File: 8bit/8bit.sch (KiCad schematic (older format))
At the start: 0 parts

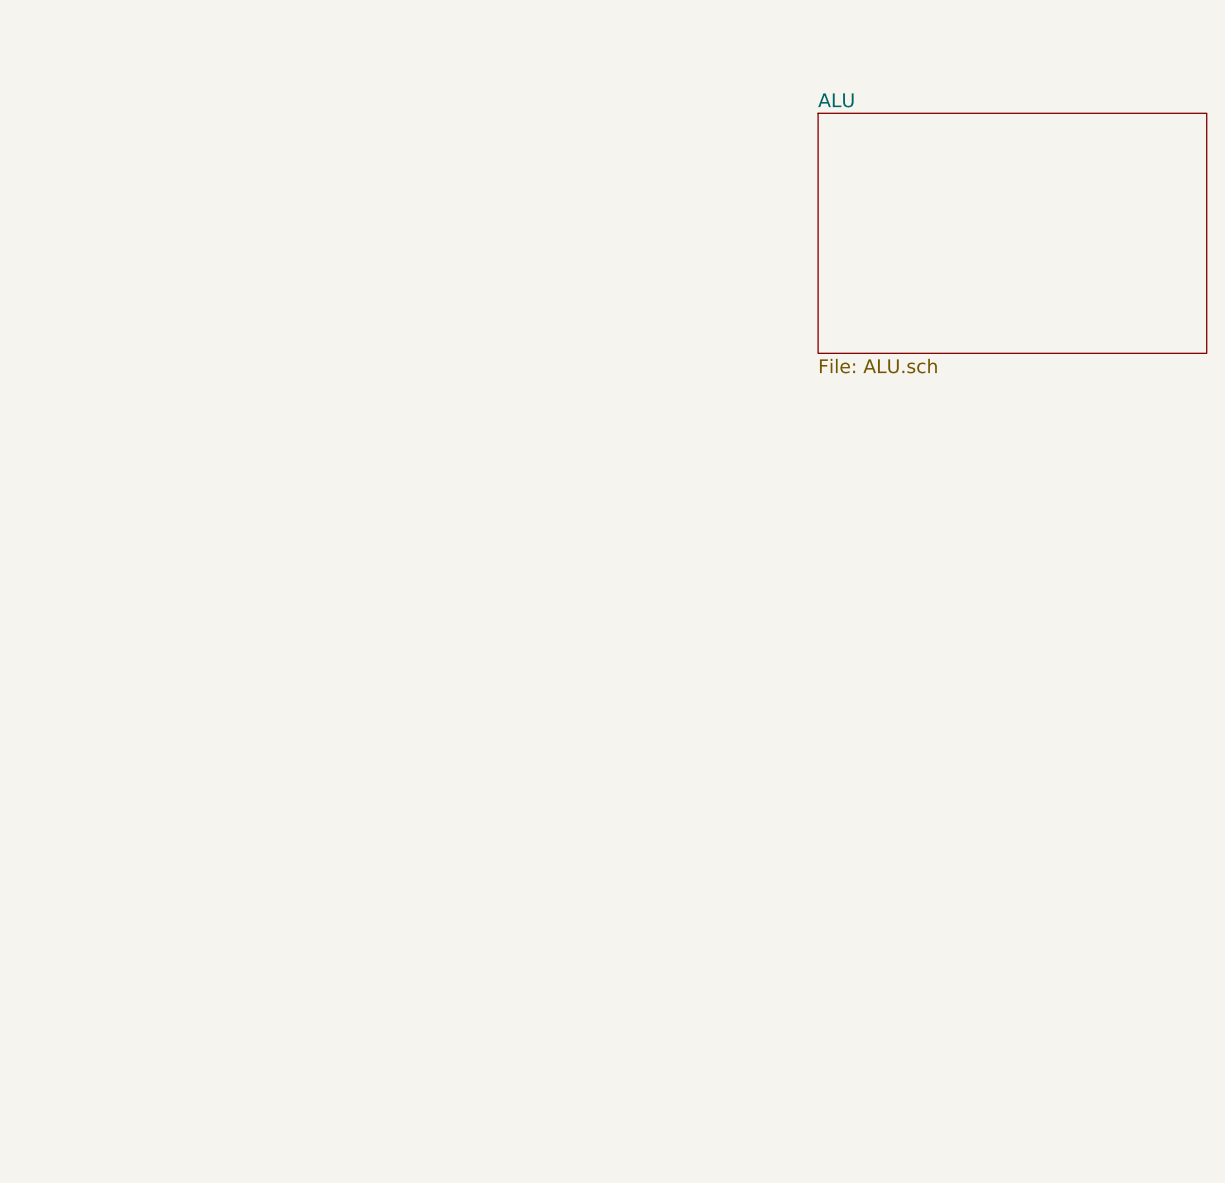
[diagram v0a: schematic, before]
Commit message: Added top level hierarchical diagram
Created 1-bit counter
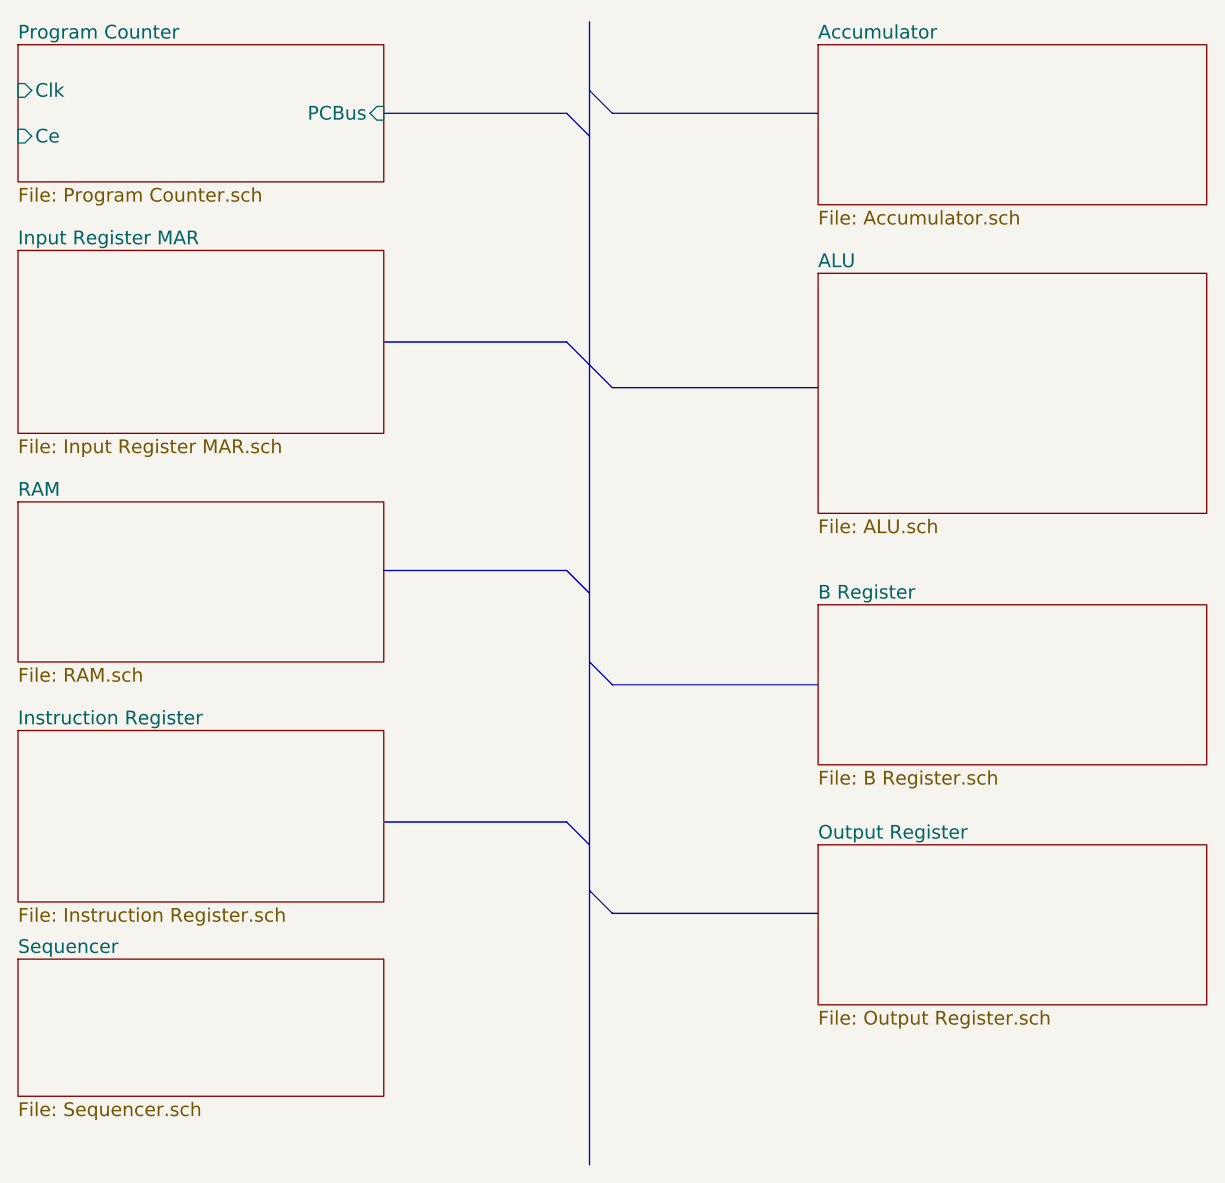
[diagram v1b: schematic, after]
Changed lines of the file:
@@
 $Descr A4 11693 8268
 encoding utf-8
-Sheet 1 11
+Sheet 1 27
 Title ""
 Date ""
@@
 $EndDescr
 $Sheet
-S 7000 2000 1700 1050
+S 7000 2700 1700 1050
 U 54949869
 F0 "ALU" 60
 F1 "ALU.sch" 60
 $EndSheet
+$Sheet
+S 7000 1700 1700 700
+U 54971ED8
+F0 "Accumulator" 60
+F1 "Accumulator.sch" 60
+$EndSheet
+$Sheet
+S 7000 4150 1700 700
+U 54971EDB
+F0 "B Register" 60
+F1 "B Register.sch" 60
+$EndSheet
+$Sheet
+S 7000 5200 1700 700
+U 54971EE2
+F0 "Output Register" 60
+F1 "Output Register.sch" 60
+$EndSheet
+$Sheet
+S 3500 1700 1600 600
+U 54971EE5
+F0 "Program Counter" 60
+F1 "Program Counter.sch" 60
+F2 "Clk" I L 3500 1900 60
+F3 "Ce" I L 3500 2100 60
+F4 "PCBus" I R 5100 2000 60
+$EndSheet
+$Sheet
+S 3500 2600 1600 800
+U 54971EEA
+F0 "Input Register MAR" 60
+F1 "Input Register MAR.sch" 60
+$EndSheet
+$Sheet
+S 3500 3700 1600 700
+U 54971F0A
+F0 "RAM" 60
+F1 "RAM.sch" 60
+$EndSheet
+$Sheet
+S 3500 4700 1600 750
+U 54971F1D
+F0 "Instruction Register" 60
+F1 "Instruction Register.sch" 60
+$EndSheet
+$Sheet
+S 3500 5700 1600 600
+U 54971F39
+F0 "Sequencer" 60
+F1 "Sequencer.sch" 60
+$EndSheet
+Wire Bus Line
+	6000 1600 6000 1900
+Wire Bus Line
+	6000 1900 6000 2100
+Wire Bus Line
+	6000 2100 6000 3100
+Wire Bus Line
+	6000 3100 6000 4100
+Wire Bus Line
+	6000 4100 6000 4400
+Wire Bus Line
+	6000 4400 6000 5200
+Wire Bus Line
+	6000 5200 6000 5400
+Wire Bus Line
+	6000 5400 6000 6600
+Entry Bus Bus
+	5900 2000 6000 2100
+Entry Bus Bus
+	6000 1900 6100 2000
+Entry Bus Bus
+	5900 3000 6000 3100
+Entry Bus Bus
+	6000 3100 6100 3200
+Entry Bus Bus
+	5900 4000 6000 4100
+Entry Bus Bus
+	6000 4400 6100 4500
+Entry Bus Bus
+	5900 5100 6000 5200
+Entry Bus Bus
+	6000 5400 6100 5500
+Wire Bus Line
+	5900 2000 5100 2000
+Wire Bus Line
+	6100 2000 7000 2000
+Wire Bus Line
+	6100 3200 7000 3200
+Wire Bus Line
+	5900 3000 5100 3000
+Wire Bus Line
+	5100 4000 5900 4000
+Wire Bus Line
+	6100 4500 7000 4500
+Wire Bus Line
+	5900 5100 5100 5100
+Wire Bus Line
+	6100 5500 7000 5500
 $EndSCHEMATC
